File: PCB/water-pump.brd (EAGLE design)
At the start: 53 x 79.1 mm, 29 parts, among them U1 LDL1117S12R, U3 ATSAMD11C14A-SSUT

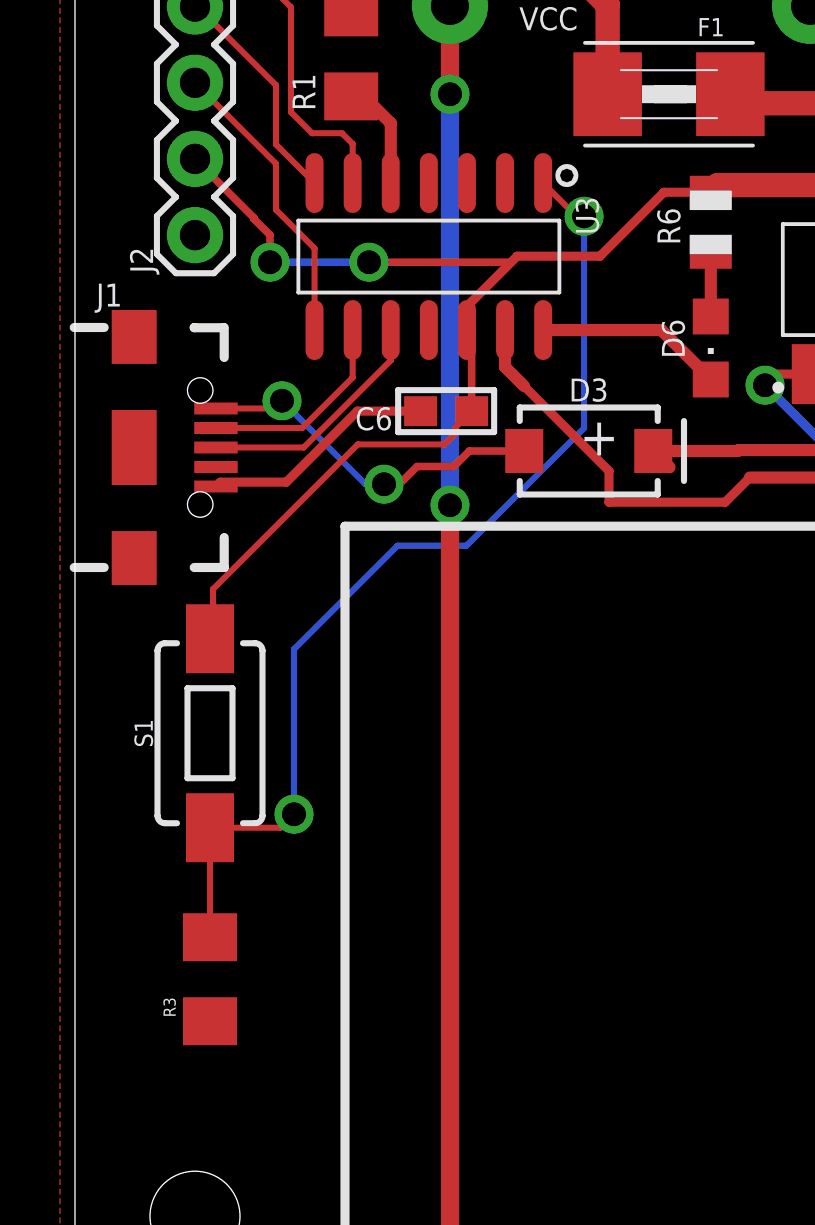
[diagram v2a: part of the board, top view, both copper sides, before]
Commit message: removed buttons.. not needed
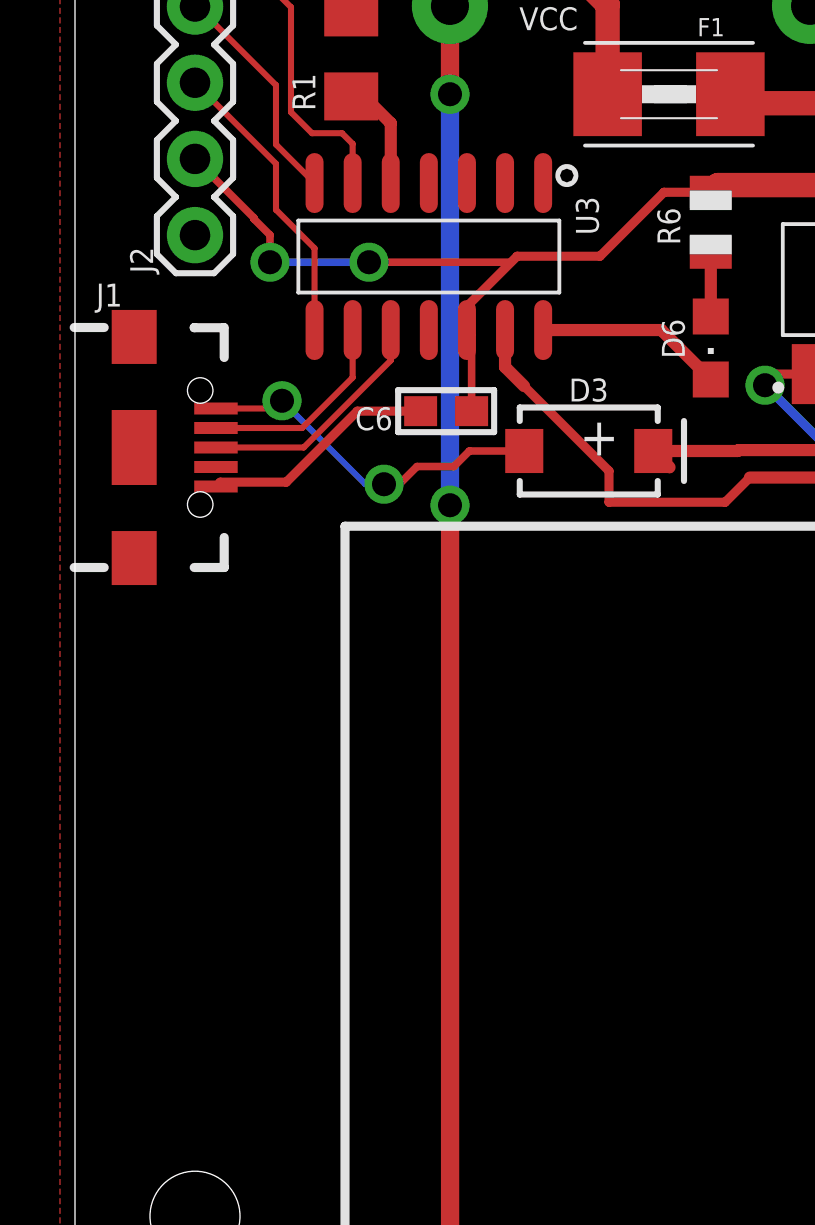
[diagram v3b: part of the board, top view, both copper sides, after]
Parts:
- removed R3: 2k, SparkFun-Resistors:1206
- removed S1: MOMENTARY-SWITCH-SPST-SMD-6.0X3.5MM, SparkFun-Switches:TACTILE_SWITCH_SMD_6.0X3.5MM
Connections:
- removed net N$4: R3.2, S1.1, U3.1
- net 3.3V: no longer S1.2
- net GND: no longer R3.1
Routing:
- net N$4: track 33.7 -> 0.00 mm, vias 2 -> 0
- net 3.3V: track 56.4 -> 43.5 mm
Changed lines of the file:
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@@
 <attribute name="VALUE" x="21.6575" y="65.495" size="0.6096" layer="27" rot="R180"/>
-</element>
-<element name="R3" library="SparkFun-Resistors" package="1206" value="2k" x="4.5" y="37.9" smashed="yes" rot="R90">
-<attribute name="NAME" x="3.357" y="36.63" size="0.4064" layer="25" rot="R90"/>
-<attribute name="VALUE" x="6.024" y="36.503" size="0.4064" layer="27" rot="R90"/>
-</element>
-<element name="S1" library="SparkFun-Switches" package="TACTILE_SWITCH_SMD_6.0X3.5MM" value="MOMENTARY-SWITCH-SPST-SMD-6.0X3.5MM" x="4.5" y="46.1" smashed="yes" rot="R90">
-<attribute name="NAME" x="2.595" y="46.1" size="0.6096" layer="25" font="vector" ratio="20" rot="R90" align="bottom-center"/>
-<attribute name="PROD_ID" value="SWCH-00815" x="4.5" y="46.1" size="1.778" layer="27" rot="R90" display="off"/>
-<attribute name="SF_SKU" value="COM-08229" x="4.5" y="46.1" size="1.778" layer="27" rot="R90" display="off"/>
 </element>
 <element name="R4" library="SparkFun-Resistors" package="1206" value="499R" x="40" y="55.3" smashed="yes" rot="R180">
@@
 <contactref element="Q1" pad="2"/>
 <contactref element="J1" pad="GND"/>
-<contactref element="R3" pad="1"/>
 <wire x1="9.53020625" y1="56.836" x2="11.521" y2="56.836" width="0.2032" layer="1"/>
 <wire x1="4.699" y1="54.324" x2="4.8442" y2="54.4692" width="0.3048" layer="1"/>
@@
 <wire x1="23" y1="57.7" x2="23.371" y2="58.071" width="0.3048" layer="1"/>
 <wire x1="23.371" y1="58.071" x2="24.643" y2="58.071" width="0.3048" layer="1"/>
+<wire x1="40.502" y1="75.646" x2="43.15" y2="73" width="0" layer="19" extent="1-1"/>
+<wire x1="37.85" y1="73" x2="40.502" y2="75.646" width="0" layer="19" extent="1-1"/>
+<wire x1="40.502" y1="70.346" x2="43.15" y2="73" width="0" layer="19" extent="1-1"/>
+<wire x1="32.221" y1="62.553" x2="40.502" y2="70.346" width="0" layer="19" extent="1-1"/>
+<wire x1="32.973" y1="56.217" x2="32.221" y2="62.553" width="0" layer="19" extent="1-1"/>
+<wire x1="11.795" y1="59.539" x2="23" y2="57.7" width="0" layer="19" extent="1-16"/>
+<wire x1="11.521" y1="56.836" x2="11.795" y2="59.539" width="0" layer="19" extent="1-1"/>
+<wire x1="1.974" y1="55.624" x2="4.699" y2="54.324" width="0" layer="19" extent="1-1"/>
+<wire x1="1.974" y1="51.939" x2="4.699" y2="54.324" width="0" layer="19" extent="1-1"/>
+<wire x1="1.974" y1="59.309" x2="1.974" y2="55.624" width="0" layer="19" extent="1-1"/>
+<wire x1="4" y1="62.703" x2="1.974" y2="59.309" width="0" layer="19" extent="1-1"/>
+<wire x1="49.034" y1="59.609" x2="40.502" y2="70.346" width="0" layer="19" extent="1-1"/>
+<wire x1="49.317" y1="51.784" x2="49.034" y2="59.609" width="0" layer="19" extent="1-1"/>
+<wire x1="40.502" y1="9.146" x2="49.317" y2="51.784" width="0" layer="19" extent="1-1"/>
+<wire x1="43.15" y1="6.5" x2="40.502" y2="9.146" width="0" layer="19" extent="1-1"/>
+<wire x1="37.85" y1="6.5" x2="40.502" y2="9.146" width="0" layer="19" extent="1-1"/>
+<wire x1="40.502" y1="3.846" x2="43.15" y2="6.5" width="0" layer="19" extent="1-1"/>
 </signal>
 <signal name="VCC-RAW" class="1">
@@
 <wire x1="9.8" y1="61.8" x2="14.5377875" y2="61.8" width="0.254" layer="1"/>
 <wire x1="14.5377875" y1="61.8" x2="14.7377875" y2="62" width="0.254" layer="1"/>
-<contactref element="S1" pad="2"/>
-<wire x1="4.5" y1="49.25" x2="4.6" y2="49.35" width="0.2032" layer="1"/>
-<wire x1="4.6" y1="49.35" x2="4.6" y2="50.9" width="0.2032" layer="1"/>
-<wire x1="12.32350625" y1="55.7264" x2="12.6806" y2="56.08349375" width="0.2032" layer="1"/>
-<wire x1="4.6" y1="50.9" x2="9.4264" y2="55.7264" width="0.2032" layer="1"/>
-<wire x1="12.6806" y1="56.08349375" x2="12.6806" y2="56.2956" width="0.2032" layer="1"/>
-<wire x1="12.6806" y1="56.2956" x2="13.221" y2="56.836" width="0.2032" layer="1"/>
-<wire x1="9.4264" y1="55.7264" x2="12.32350625" y2="55.7264" width="0.2032" layer="1"/>
 <wire x1="26.943" y1="58.071" x2="26.943" y2="64.371" width="0.2032" layer="1"/>
 </signal>
-<signal name="N$4">
-<contactref element="R3" pad="2"/>
-<contactref element="S1" pad="1"/>
-<contactref element="U3" pad="1"/>
-<wire x1="15.605" y1="64.439" x2="16.714578125" y2="63.329421875" width="0.2032" layer="1"/>
-<wire x1="16.714578125" y1="63.329421875" x2="16.970578125" y2="63.329421875" width="0.2032" layer="1"/>
-<via x="16.970578125" y="63.329421875" extent="1-16" drill="0.8"/>
-<wire x1="16.970578125" y1="56.270578125" x2="16.970578125" y2="63.329421875" width="0.2032" layer="16"/>
-<wire x1="13.05" y1="52.35" x2="16.970578125" y2="56.270578125" width="0.2032" layer="16"/>
-<via x="7.3" y="43.4" extent="1-16" drill="0.8"/>
-<wire x1="7.3" y1="43.4" x2="6.85" y2="42.95" width="0.2032" layer="1"/>
-<wire x1="6.85" y1="42.95" x2="4.5" y2="42.95" width="0.2032" layer="1"/>
-<wire x1="4.5" y1="42.95" x2="4.5" y2="39.3" width="0.2032" layer="1"/>
-<wire x1="10.75" y1="52.35" x2="13.05" y2="52.35" width="0.2032" layer="16"/>
-<wire x1="7.3" y1="43.4" x2="7.3" y2="48.9" width="0.2032" layer="16"/>
-<wire x1="7.3" y1="48.9" x2="10.75" y2="52.35" width="0.2032" layer="16"/>
-</signal>
 <signal name="N$5">

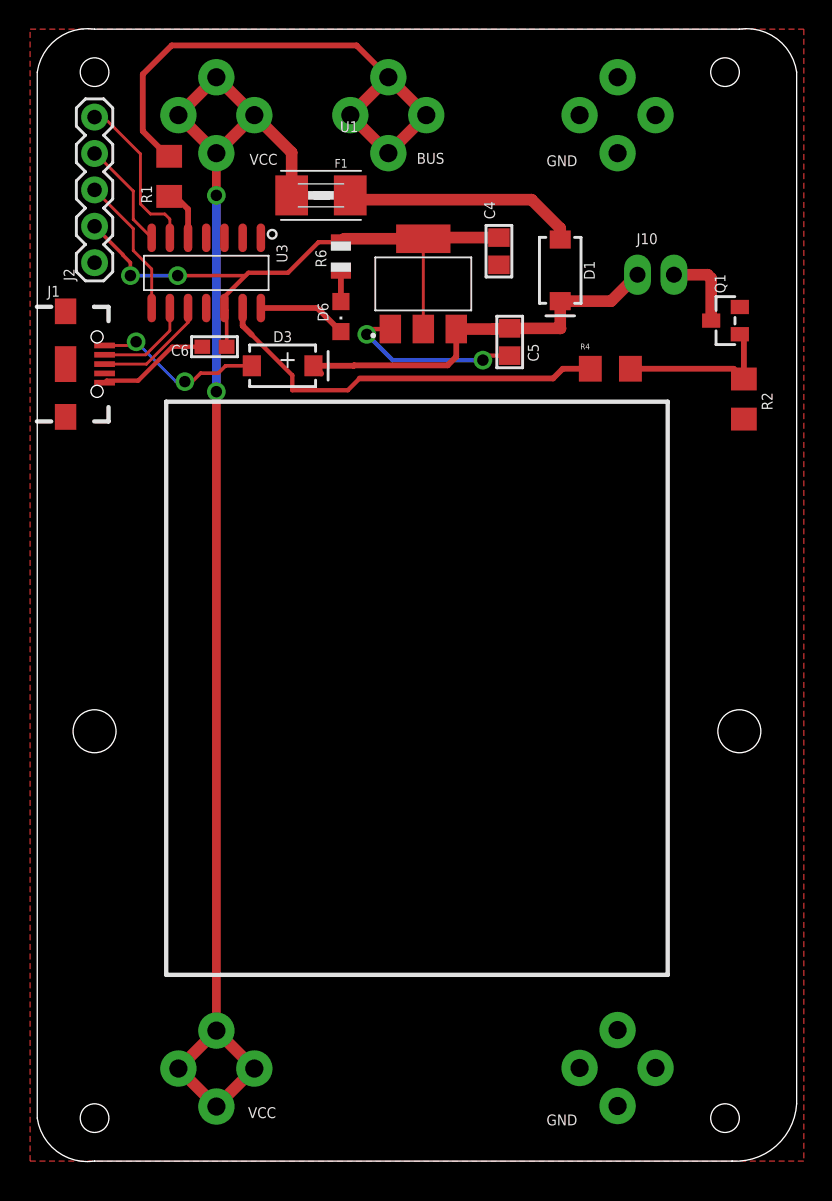
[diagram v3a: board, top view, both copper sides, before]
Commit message: shrinked water pump pcb in length
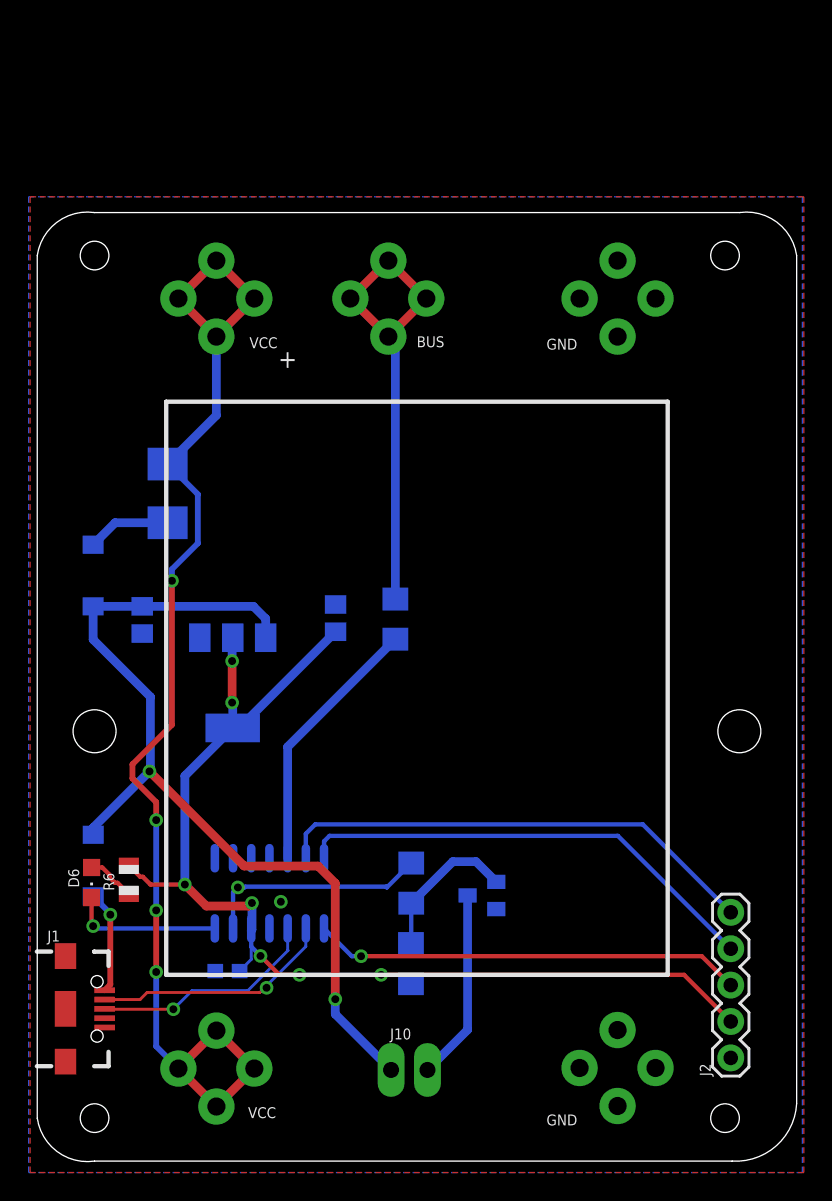
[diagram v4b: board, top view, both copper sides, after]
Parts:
- moved J2 71.1 mm to (48.4, 7.20)
- moved J10 58.1 mm to (24.7, 6.36)
- moved R6 45.9 mm to (6.39, 19.6)
- moved R2 45.7 mm to (26.1, 13.8), flipped to the bottom
- moved J1 45.0 mm to (1.97, 10.6)
- moved C6 43.6 mm to (13.3, 13.3), flipped to the bottom, turned to 0 degrees
- moved Q1 43.6 mm to (31.0, 18.5), flipped to the bottom, turned to 270 degrees
- moved U3 43.5 mm to (16.2, 18.7), flipped to the bottom
- moved D6 43.2 mm to (3.79, 19.4)
- moved D1 38.9 mm to (3.90, 40.9), flipped to the bottom
- moved R4 38.5 mm to (26.1, 19.4), flipped to the bottom, turned to 90 degrees
- moved D3 37.3 mm to (3.91, 20.6), flipped to the bottom, turned to 90 degrees
- moved R1 34.7 mm to (25.0, 37.8), flipped to the bottom
- moved C5 32.2 mm to (7.33, 37.8), flipped to the bottom
- moved U1 30.9 mm to (13.6, 33.4), flipped to the bottom, turned to 180 degrees
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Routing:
- net 3.3V: track 43.5 -> 80.4 mm, vias 2 -> 7
- net VCC: track 28.3 -> 63.9 mm, vias 0 -> 2
- net SWCLK: track 7.58 -> 33.0 mm
- net RESET: track 11.6 -> 34.2 mm
- net GND: track 22.5 -> 0.00 mm, vias 2 -> 1
- net SWDIO: track 9.89 -> 30.0 mm, vias 0 -> 1
- net N$3: track 3.92 -> 18.4 mm
- net PUMP_CTRL: track 28.6 -> 15.8 mm, vias 0 -> 1
- net VCC-RAW: track 97.9 -> 86.6 mm, vias 2 -> 4
- net N$6: track 16.4 -> 5.84 mm
- net USB-: track 6.84 -> 16.9 mm, vias 0 -> 1
- net USB+: track 8.04 -> 16.1 mm, vias 0 -> 1
- net PUMP: track 5.65 -> 13.3 mm
- net BUS: track 40.4 -> 33.5 mm
- net N$1: track 12.0 -> 7.21 mm, vias 2 -> 1
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- added copper zone on layer 16, net GND
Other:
- board size 53 x 79.1 mm -> 53 x 66.3 mm
